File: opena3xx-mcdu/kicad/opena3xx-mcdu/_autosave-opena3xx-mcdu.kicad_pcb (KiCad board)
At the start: 2 copper layers, 145.3 x 224.3 mm, 145 parts, among them J1 Conn_02x01, J2 Conn_02x01, J3 Conn_02x01, J4 Conn_02x01, J5 Conn_02x01, J6 Conn_02x01, J7 Conn_02x01, J8 Conn_02x01, J9 Conn_02x01, SW1 TLL-6A, SW10 TLL-6A, SW100 SW_MEC_5E, SW11 TLL-6A, SW12 TLL-6A, SW13 TLL-6A, SW14 TLL-6A, SW15 TLL-6A, SW16 TLL-6A, SW17 TLL-6A, SW18 TLL-6A, SW19 TLL-6A, SW2 TLL-6A, SW20 TLL-6A, SW21 TLL-6A, SW22 TLL-6A, SW23 TLL-6A, SW24 TLL-6A, SW25 TLL-6A, SW26 TLL-6A, SW27 TLL-6A, SW28 TLL-6A, SW29 TLL-6A, SW3 TLL-6A, SW30 TLL-6A, SW31 TLL-6A, SW32 TLL-6A, SW33 TLL-6A, SW34 TLL-6A, SW35 TLL-6A, SW36 TLL-6A, SW37 TLL-6A, SW38 TLL-6A, SW39 TLL-6A, SW4 TLL-6A, SW40 TLL-6A, SW41 TLL-6A, SW42 TLL-6A, SW43 TLL-6A, SW44 TLL-6A, SW45 TLL-6A, SW46 TLL-6A, SW47 TLL-6A, SW48 TLL-6A, SW49 TLL-6A, SW5 TLL-6A, SW50 TLL-6A, SW51 TLL-6A, SW52 TLL-6A, SW53 TLL-6A, SW54 TLL-6A, SW55 TLL-6A, SW56 TLL-6A, SW57 TLL-6A, SW58 TLL-6A, SW59 TLL-6A, SW6 TLL-6A, SW60 TLL-6A, SW61 TLL-6A, SW62 TLL-6A, SW63 TLL-6A, SW64 TLL-6A, SW65 TLL-6A, SW66 TLL-6A, SW67 TLL-6A, SW68 TLL-6A, SW69 TLL-6A, SW7 TLL-6A, SW70 TLL-6A, SW8 TLL-6A, SW9 TLL-6A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

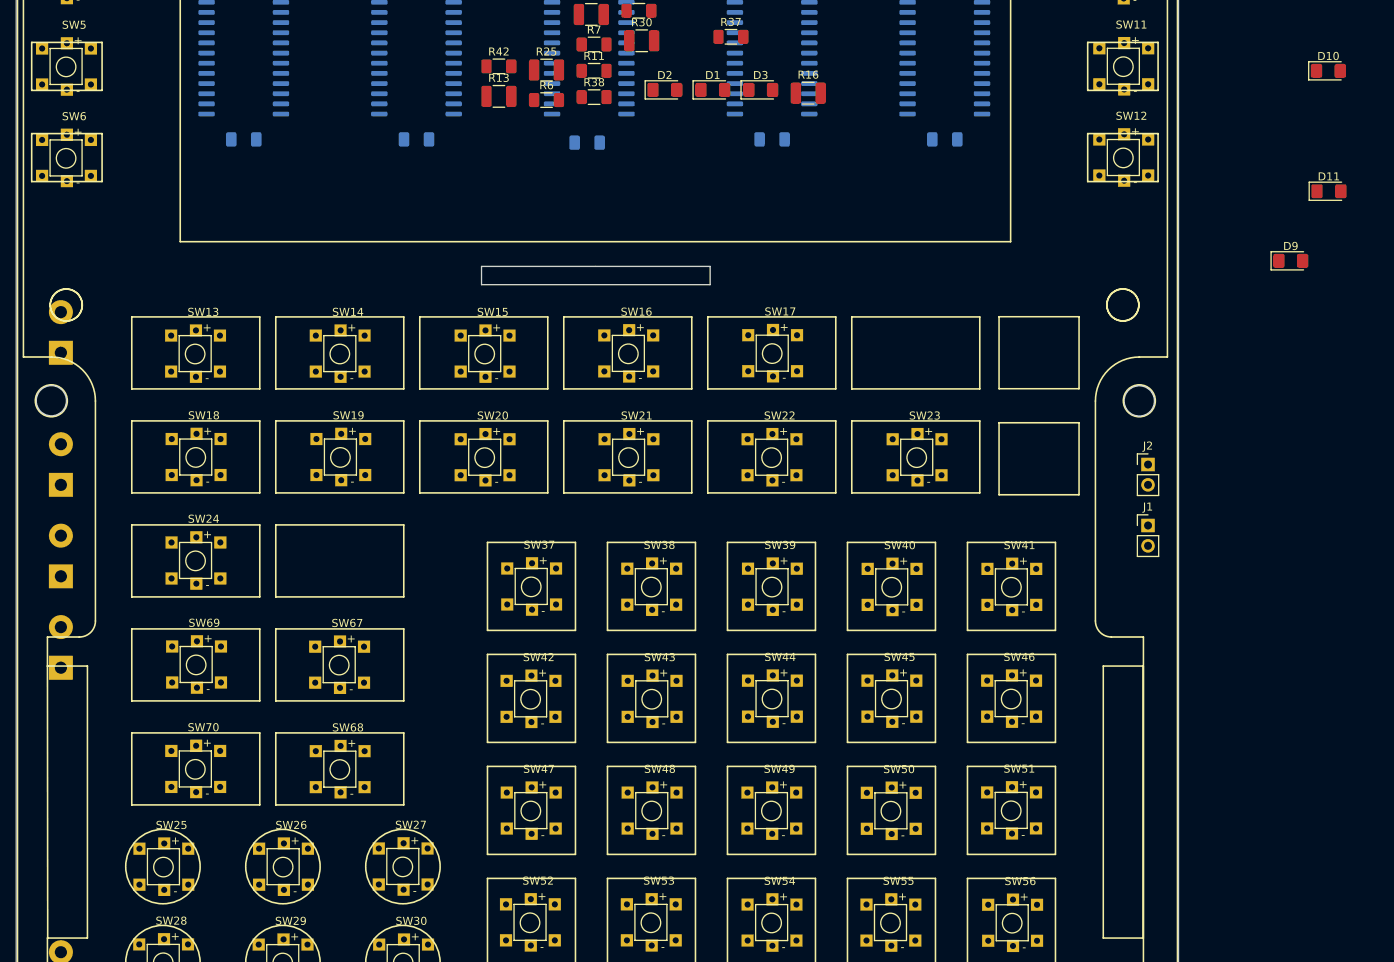
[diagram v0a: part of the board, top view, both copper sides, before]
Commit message: Adding Contributing.md Minor imporvements to PCB
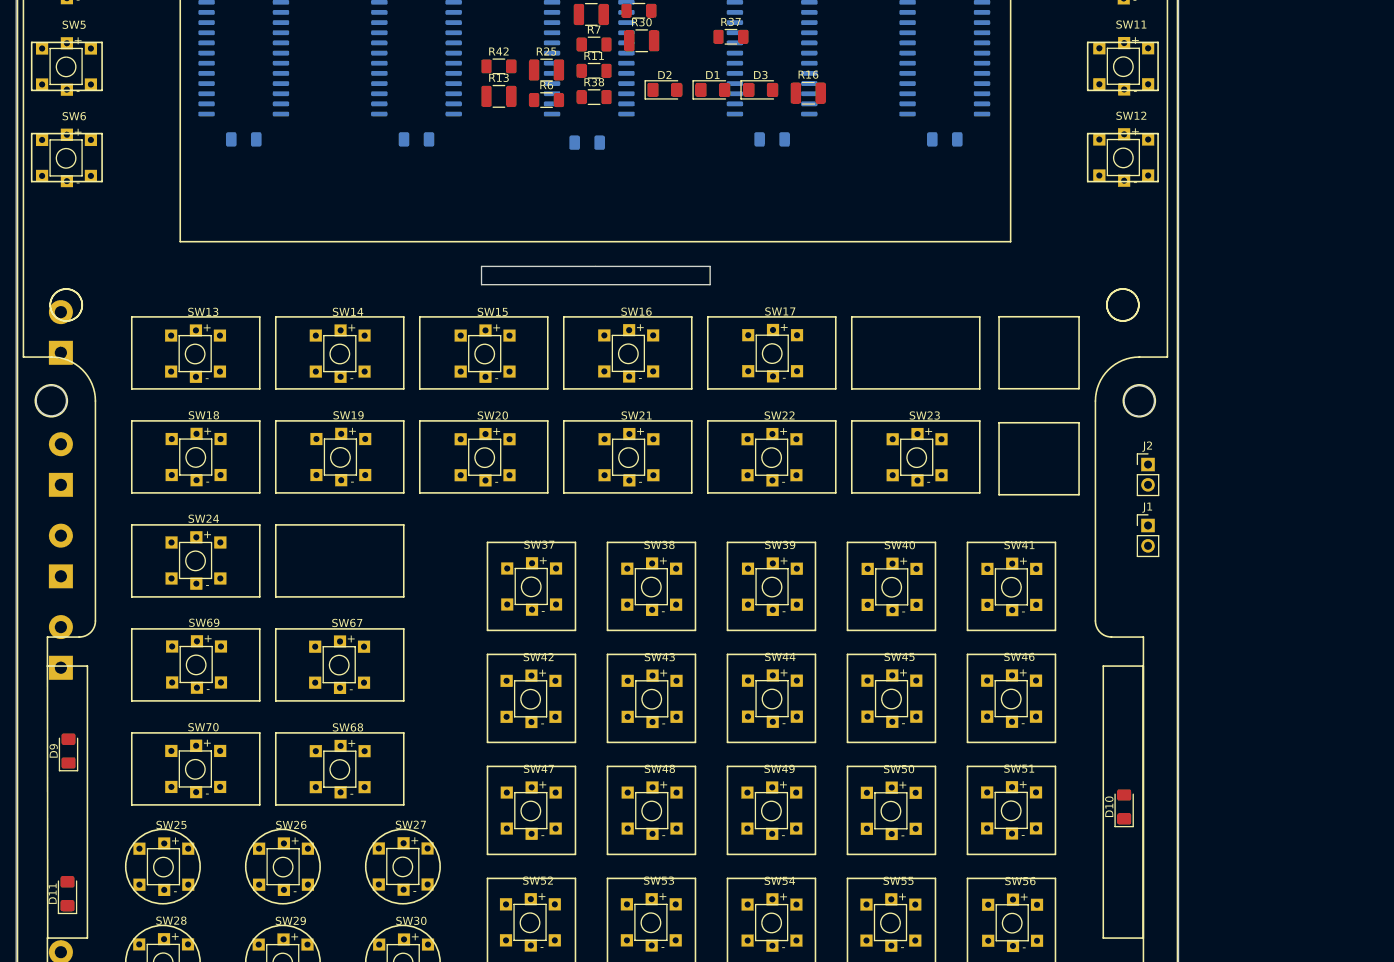
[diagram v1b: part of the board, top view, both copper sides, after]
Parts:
- moved D11 180.5 mm to (139.6, 209.8), turned to 90 degrees
- moved D9 164.6 mm to (139.8, 192.0), turned to 90 degrees
- moved D10 95.5 mm to (271.7, 199.0), turned to 90 degrees
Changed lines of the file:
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@@
   )
   (module Diode_SMD:D_1206_3216Metric_Pad1.42x1.75mm_HandSolder (layer F.Cu)
-    (at 297.307 121.9962)
+    (at 139.6365 209.8167 90)
     (descr "Diode SMD 1206 (3216 Metric), square (rectangular) end terminal, IPC_7351 nominal, (Body size source: http://www.tortai-tech.com/upload/download/2011102023233369053.pdf), generated with kicad-footprint-generator")
     (tags "diode handsolder")
     (attr smd)
-    (fp_text reference D11 (at 0 -1.82) (layer F.SilkS)
+    (fp_text reference D11 (at 0 -1.82 90) (layer F.SilkS)
       (effects (font (size 1 1) (thickness 0.15)))
     )
-    (fp_text value "FM - White LED" (at 0 1.82) (layer F.Fab)
+    (fp_text value "FM - White LED" (at 0 1.82 90) (layer F.Fab)
       (effects (font (size 1 1) (thickness 0.15)))
     )
@@
     (fp_line (start -1.2 -0.8) (end -1.6 -0.4) (layer F.Fab) (width 0.1))
     (fp_line (start 1.6 -0.8) (end -1.2 -0.8) (layer F.Fab) (width 0.1))
-    (fp_text user %R (at 0 0) (layer F.Fab)
+    (fp_text user %R (at 0 0 90) (layer F.Fab)
       (effects (font (size 0.8 0.8) (thickness 0.12)))
     )
-    (pad 2 smd roundrect (at 1.4875 0) (size 1.425 1.75) (layers F.Cu F.Paste F.Mask) (roundrect_rratio 0.175439)
+    (pad 2 smd roundrect (at 1.4875 0 90) (size 1.425 1.75) (layers F.Cu F.Paste F.Mask) (roundrect_rratio 0.175439)
       (net 96 /BUS4-12))
-    (pad 1 smd roundrect (at -1.4875 0) (size 1.425 1.75) (layers F.Cu F.Paste F.Mask) (roundrect_rratio 0.175439)
+    (pad 1 smd roundrect (at -1.4875 0 90) (size 1.425 1.75) (layers F.Cu F.Paste F.Mask) (roundrect_rratio 0.175439)
       (net 127 "Net-(D11-Pad1)"))
     (model ${KISYS3DMOD}/Diode_SMD.3dshapes/D_1206_3216Metric.wrl
@@
   )
   (module Diode_SMD:D_1206_3216Metric_Pad1.42x1.75mm_HandSolder (layer F.Cu)
-    (at 297.2435 106.9467)
+    (at 271.7165 198.9582 90)
     (descr "Diode SMD 1206 (3216 Metric), square (rectangular) end terminal, IPC_7351 nominal, (Body size source: http://www.tortai-tech.com/upload/download/2011102023233369053.pdf), generated with kicad-footprint-generator")
     (tags "diode handsolder")
     (attr smd)
-    (fp_text reference D10 (at 0 -1.82) (layer F.SilkS)
+    (fp_text reference D10 (at 0 -1.82 90) (layer F.SilkS)
       (effects (font (size 1 1) (thickness 0.15)))
     )
-    (fp_text value "MCDU MENU - WHITE LED" (at 0 1.82) (layer F.Fab)
+    (fp_text value "MCDU MENU - WHITE LED" (at 0 1.82 90) (layer F.Fab)
       (effects (font (size 1 1) (thickness 0.15)))
     )
@@
     (fp_line (start -1.2 -0.8) (end -1.6 -0.4) (layer F.Fab) (width 0.1))
     (fp_line (start 1.6 -0.8) (end -1.2 -0.8) (layer F.Fab) (width 0.1))
-    (fp_text user %R (at 0 0) (layer F.Fab)
+    (fp_text user %R (at 0 0 90) (layer F.Fab)
       (effects (font (size 0.8 0.8) (thickness 0.12)))
     )
-    (pad 2 smd roundrect (at 1.4875 0) (size 1.425 1.75) (layers F.Cu F.Paste F.Mask) (roundrect_rratio 0.175439)
+    (pad 2 smd roundrect (at 1.4875 0 90) (size 1.425 1.75) (layers F.Cu F.Paste F.Mask) (roundrect_rratio 0.175439)
       (net 97 /BUS4-11))
-    (pad 1 smd roundrect (at -1.4875 0) (size 1.425 1.75) (layers F.Cu F.Paste F.Mask) (roundrect_rratio 0.175439)
+    (pad 1 smd roundrect (at -1.4875 0 90) (size 1.425 1.75) (layers F.Cu F.Paste F.Mask) (roundrect_rratio 0.175439)
       (net 126 "Net-(D10-Pad1)"))
     (model ${KISYS3DMOD}/Diode_SMD.3dshapes/D_1206_3216Metric.wrl
@@
   )
   (module Diode_SMD:D_1206_3216Metric_Pad1.42x1.75mm_HandSolder (layer F.Cu)
-    (at 292.5445 130.6957)
+    (at 139.7635 191.9732 90)
     (descr "Diode SMD 1206 (3216 Metric), square (rectangular) end terminal, IPC_7351 nominal, (Body size source: http://www.tortai-tech.com/upload/download/2011102023233369053.pdf), generated with kicad-footprint-generator")
     (tags "diode handsolder")
     (attr smd)
-    (fp_text reference D9 (at 0 -1.82) (layer F.SilkS)
+    (fp_text reference D9 (at 0 -1.82 90) (layer F.SilkS)
       (effects (font (size 1 1) (thickness 0.15)))
     )
-    (fp_text value "FAIL - Amber LED" (at 0 1.82) (layer F.Fab)
+    (fp_text value "FAIL - Amber LED" (at 0 1.82 90) (layer F.Fab)
       (effects (font (size 1 1) (thickness 0.15)))
     )
@@
     (fp_line (start -1.2 -0.8) (end -1.6 -0.4) (layer F.Fab) (width 0.1))
     (fp_line (start 1.6 -0.8) (end -1.2 -0.8) (layer F.Fab) (width 0.1))
-    (fp_text user %R (at 0 0) (layer F.Fab)
+    (fp_text user %R (at 0 0 90) (layer F.Fab)
       (effects (font (size 0.8 0.8) (thickness 0.12)))
     )
-    (pad 2 smd roundrect (at 1.4875 0) (size 1.425 1.75) (layers F.Cu F.Paste F.Mask) (roundrect_rratio 0.175439)
+    (pad 2 smd roundrect (at 1.4875 0 90) (size 1.425 1.75) (layers F.Cu F.Paste F.Mask) (roundrect_rratio 0.175439)
       (net 98 /BUS4-10))
-    (pad 1 smd roundrect (at -1.4875 0) (size 1.425 1.75) (layers F.Cu F.Paste F.Mask) (roundrect_rratio 0.175439)
+    (pad 1 smd roundrect (at -1.4875 0 90) (size 1.425 1.75) (layers F.Cu F.Paste F.Mask) (roundrect_rratio 0.175439)
       (net 125 "Net-(D9-Pad1)"))
     (model ${KISYS3DMOD}/Diode_SMD.3dshapes/D_1206_3216Metric.wrl
